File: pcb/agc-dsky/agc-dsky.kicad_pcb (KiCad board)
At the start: 2 copper layers, 100 x 115 mm, 152 parts, among them IC1 TPS62132, IC10 LDS-3161AX, IC11 LDS-3161AX, IC12 LDS-3161AX, IC13 LDS-3161AX, IC14 LDS-3161AX, IC15 LDS-3161AX, IC16 LDS-3161AX, IC17 LDS-3161AX, IC18 LDS-3161AX, IC19 LDS-3161AX, IC2 STM32F072RBT6, IC20 LDS-3161AX, IC21 LDS-3161AX, IC22 LDS-3161AX, IC23 LDS-3161AX, IC24 LDS-3161AX, IC25 LDS-3161AX, IC26 LDS-3161AX, IC27 WS2812B, IC28 WS2812B, IC29 WS2812B, IC3 MCP23S08, IC30 WS2812B, IC31 WS2812B, IC32 WS2812B, IC33 WS2812B, IC34 WS2812B, IC35 WS2812B, IC36 WS2812B, IC37 WS2812B, IC38 WS2812B, IC39 WS2812B, IC4 MCP23S08, IC5 MCP23S08, IC6 LDS-3161AX, IC7 LDS-3161AX, IC8 LDS-3161AX, IC9 LDS-3161AX, J1 MICROUSB, P1 SWD_TC, Q1 FDN327N, Q2 FDN327N, Q3 FDN327N, Q4 FDN327N, Q5 FDN327N, Q6 FDN327N, Q7 FDN327N, Q8 FDN327N, SW1 SKPMAME010, SW10 SKPMAME010, SW11 SKPMAME010, SW12 SKPMAME010, SW13 SKPMAME010, SW14 SKPMAME010, SW15 SKPMAME010, SW16 SKPMAME010, SW17 SKPMAME010, SW18 SKPMAME010, SW19 SKPMAME010, SW2 SKPMAME010, SW20 SKPMAME010, SW3 SKPMAME010, SW4 SKPMAME010, SW5 SKPMAME010, SW6 SKPMAME010, SW7 SKPMAME010, SW8 SKPMAME010, SW9 SKHHALA010

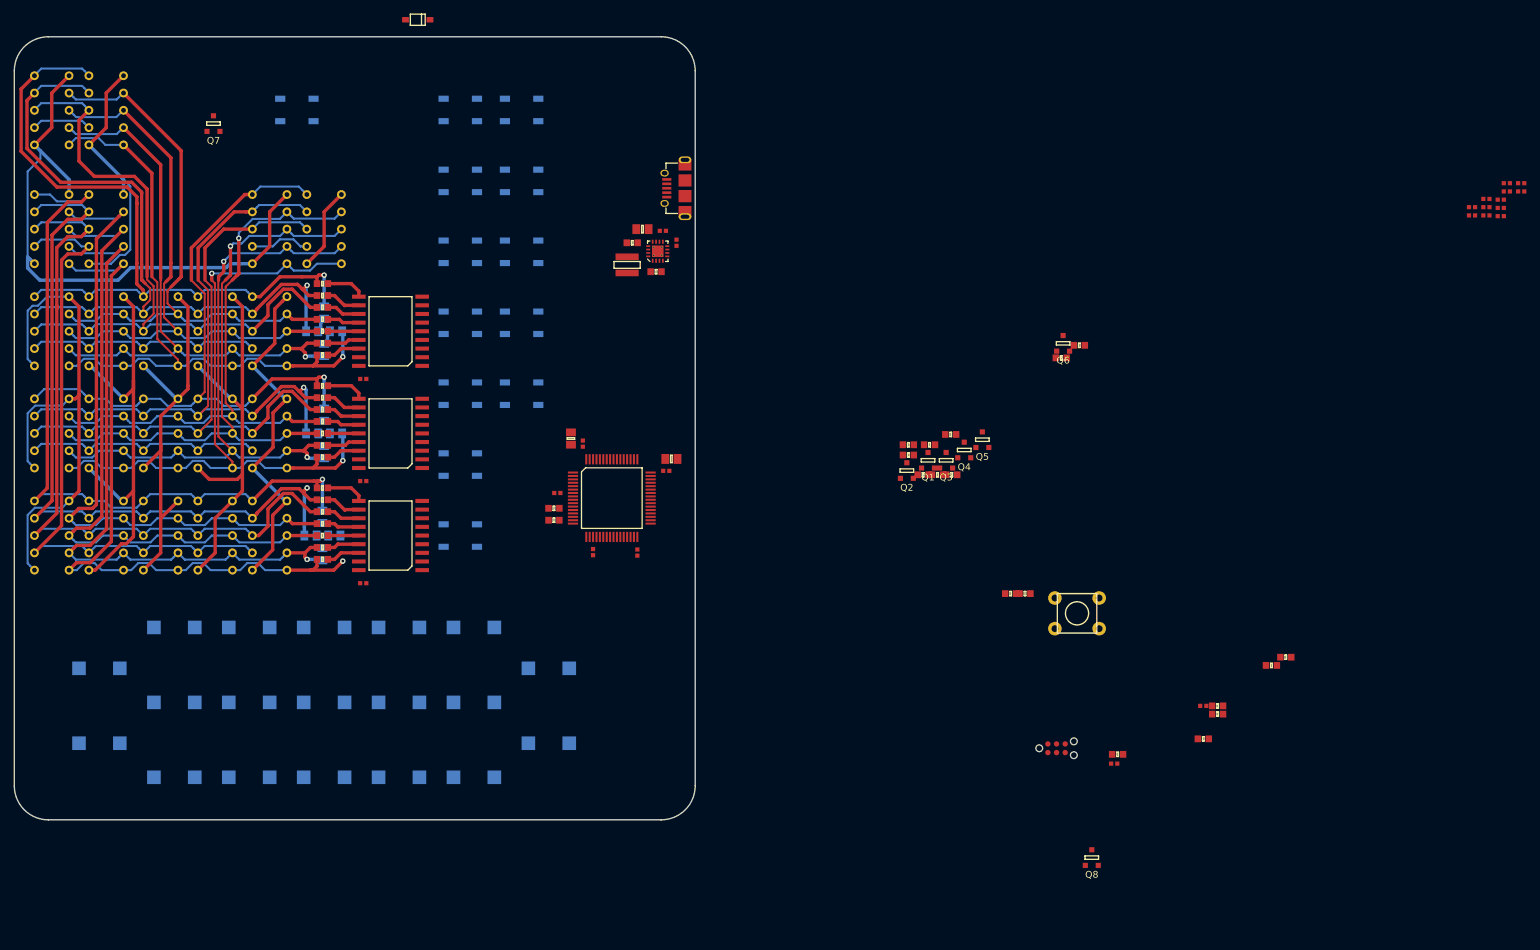
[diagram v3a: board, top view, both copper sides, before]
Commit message: Add ground pour on bottom layer
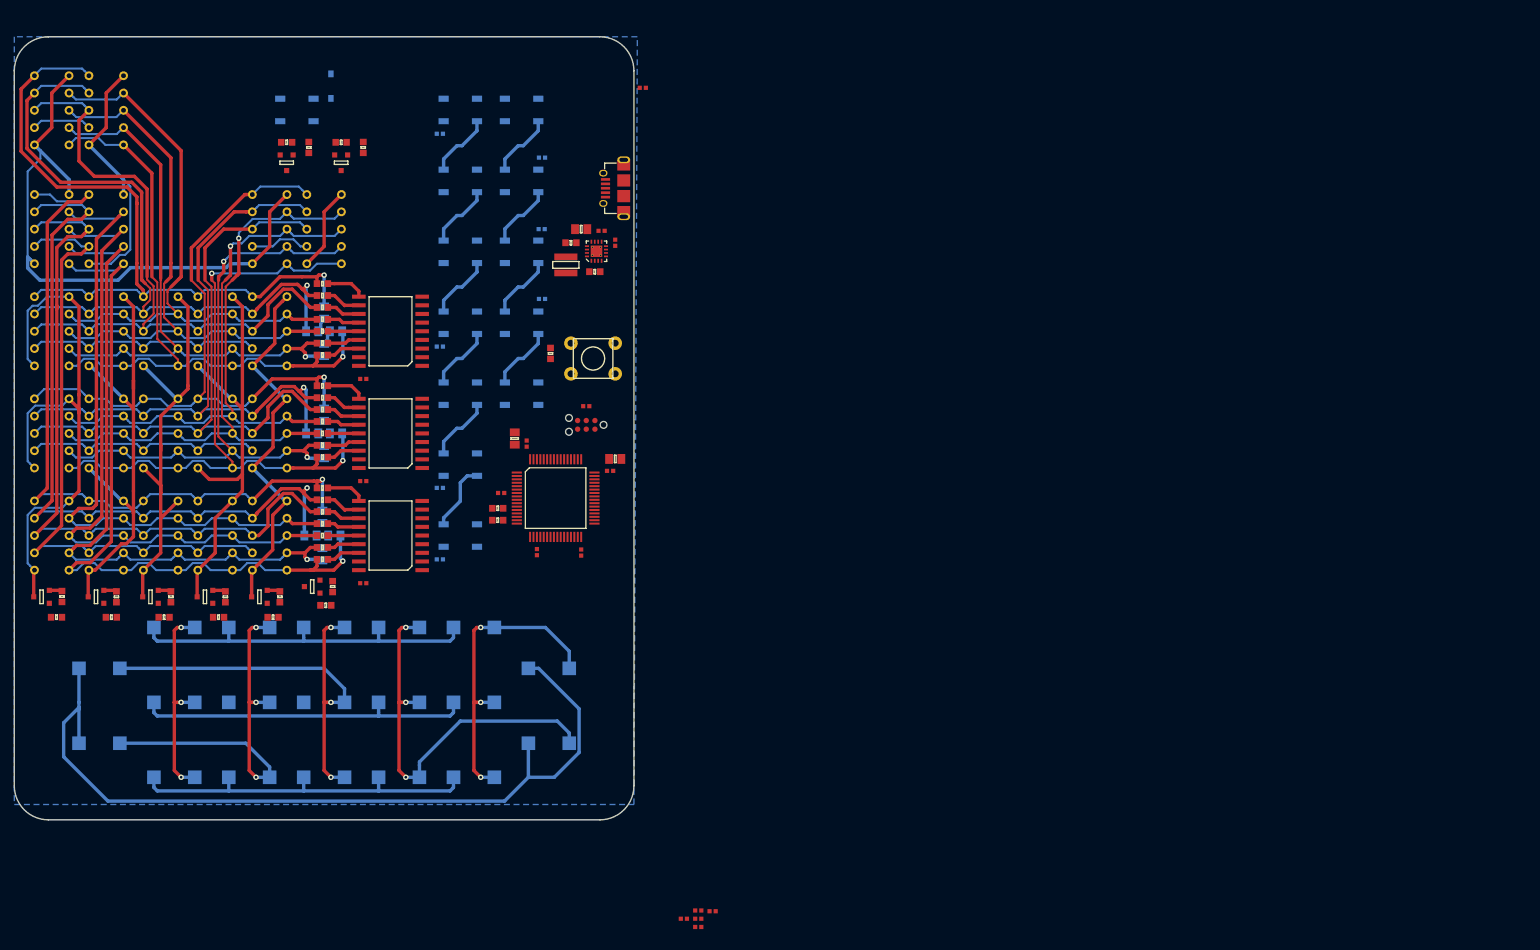
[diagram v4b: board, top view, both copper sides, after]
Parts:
- C19, C20, C21, C24, C25, C27, C30, D13: moved to B.Cu
- moved R30 170.5 mm to (73.0, 115.2), turned to 180 degrees
- moved C24 168.1 mm to (121.2, 106.8), turned to 180 degrees
- moved R29 164.0 mm to (81.8, 112.2), turned to 90 degrees
- moved C27 158.3 mm to (121.2, 75.5), turned to 180 degrees
- moved C30 156.9 mm to (121.2, 44.2), turned to 180 degrees
- moved C25 156.8 mm to (121.2, 96.2), turned to 180 degrees
- moved C23 155.9 mm to (159.2, 160.7)
- moved C22 155.9 mm to (161.3, 158.4)
- moved C26 155.9 mm to (159.2, 159.5)
- moved C29 155.9 mm to (159.2, 158.3)
- moved C28 155.9 mm to (157.1, 159.5)
- moved R28 153.7 mm to (80.8, 115.2)
- moved R27 146.6 mm to (89.8, 112.2), turned to 90 degrees
- moved C19 143.9 mm to (136.2, 47.8)
- moved C21 141.3 mm to (136.2, 68.5)
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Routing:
- net /BR4: track 0.00 -> 122.1 mm
- net /BC3: track 0.00 -> 66.4 mm, vias 0 -> 3
- net /BC2: track 0.00 -> 59.1 mm, vias 0 -> 3
- net /BC4: track 0.00 -> 55.1 mm, vias 0 -> 3
- net /BR3: track 0.00 -> 53.4 mm
- net /BR1: track 0.00 -> 53.4 mm
- net /BR2: track 0.00 -> 49.4 mm
- net /BC1: track 0.00 -> 45.1 mm, vias 0 -> 3
- net /BC5: track 0.00 -> 30.2 mm, vias 0 -> 3
- net Net-(IC33-Pad2): track 0.00 -> 9.99 mm
- net Net-(IC38-Pad2): track 0.00 -> 9.59 mm
- net Net-(IC37-Pad2): track 0.00 -> 9.59 mm
- net Net-(IC36-Pad2): track 0.00 -> 9.59 mm
- net Net-(IC35-Pad2): track 0.00 -> 9.59 mm
- net Net-(IC34-Pad2): track 0.00 -> 9.59 mm
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- added copper zone on B.Cu, net GND
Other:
- board size 100 x 115 mm -> 91 x 115 mm

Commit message: More work on layout
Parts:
- C18, C22, C23, C26, C28, C29: moved to B.Cu
- moved C23 135.4 mm to (104.2, 37.0), turned to 90 degrees
- moved C29 114.3 mm to (110.8, 54.8), turned to 180 degrees
- moved C28 105.2 mm to (110.8, 65.0), turned to 180 degrees
- moved C26 88.2 mm to (110.8, 85.8), turned to 180 degrees
- moved C22 83.4 mm to (136.7, 78.8)
- moved J1 60.0 mm to (148.2, 112.2)
- moved C18 14.8 mm to (136.2, 37.2)
- moved C11 14.5 mm to (140.2, 107.0)
- moved C8 14.1 mm to (143.8, 105.8), turned to 270 degrees
- moved C10 13.8 mm to (128.2, 104.8)
- moved C6 13.4 mm to (144.5, 94.5), turned to 0 degrees
- moved C30 12.5 mm to (108.8, 42.6)
- moved C24 11.9 mm to (109.6, 104.2), turned to 90 degrees
- moved C13 11.8 mm to (127.8, 96.8), turned to 180 degrees
- moved C7 11.7 mm to (143.8, 96.2), turned to 0 degrees
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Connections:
- C10 pad 2: Net-(C10-Pad2) -> GND
- C11 pad 2: Net-(C11-Pad2) -> GND
- C12 pad 2: Net-(C12-Pad2) -> GND
- C13 pad 2: Net-(C10-Pad2) -> GND
- C6 pad 2: Net-(C10-Pad2) -> GND
- C7 pad 2: Net-(C10-Pad2) -> GND
- C8 pad 2: Net-(C11-Pad2) -> GND
- C9 pad 2: Net-(C12-Pad2) -> GND
- IC2 pad 15: (no net) -> /NCS_2
- IC2 pad 16: (no net) -> /NRST_2
- IC2 pad 24: /NRST_1 -> (no net)
- IC2 pad 25: /NCS_1 -> (no net)
- IC2 pad 26: /NRST_2 -> (no net)
- IC2 pad 27: /NCS_2 -> (no net)
- IC2 pad 28: (no net) -> /NCS_3
- IC2 pad 29: /Co8 -> /NRST_3
- IC2 pad 3: (no net) -> /Co6
- IC2 pad 30: /NRST_3 -> /Co8
- IC2 pad 33: /NCS_3 -> (no net)
- IC2 pad 37: (no net) -> /Co1
- IC2 pad 38: (no net) -> /Co2
- IC2 pad 39: /BC1 -> /Co3
- IC2 pad 4: (no net) -> /Co7
- IC2 pad 40: /BC2 -> /Co4
- IC2 pad 41: /BC3 -> /Co5
- IC2 pad 42: /BC4 -> /BR2
- IC2 pad 43: /BC5 -> /BR4
- IC2 pad 50: (no net) -> /BR3
- IC2 pad 51: (no net) -> /BR1
- IC2 pad 55: /Co1 -> /BC5
- IC2 pad 56: /Co2 -> /BC4
- IC2 pad 57: /Co3 -> /BC3
- IC2 pad 58: /Co4 -> /BC2
- IC2 pad 59: /Co5 -> /BC1
- IC2 pad 61: /Co6 -> (no net)
- IC2 pad 62: /Co7 -> (no net)
- IC2 pad 8: (no net) -> /NCS_1
- IC2 pad 9: (no net) -> /NRST_1
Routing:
- net /BR4: track 122.1 -> 17.3 mm, vias 0 -> 1
- net /Co5: track 0.00 -> 79.1 mm
- net /Co4: track 0.00 -> 69.7 mm
- net /Co3: track 0.00 -> 60.6 mm
- net 5v: track 0.00 -> 51.6 mm
- net /Co2: track 0.00 -> 51.2 mm
- net /Co1: track 0.00 -> 42.4 mm
- net /SPI1_SI: track 0.00 -> 38.5 mm, vias 0 -> 2
- net /SPI1_SO: track 0.00 -> 38.1 mm
- net /BC2: track 59.1 -> 24.1 mm, vias 3 -> 0
- net /SPI1_SCK: track 0.00 -> 32.9 mm
- net /NCS_1: track 0.00 -> 31.0 mm
- net /NRST_1: track 0.00 -> 30.2 mm
- net /Co8: track 0.00 -> 29.4 mm
- net /BR2: track 49.4 -> 78.6 mm, vias 0 -> 1
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
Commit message: More routing of buttons
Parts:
- moved SW1 4.75 mm to (126.2, 121.5)
- moved SW10 4.75 mm to (104.2, 121.5)
- moved SW11 4.75 mm to (104.2, 132.5)
- moved SW12 4.75 mm to (104.2, 143.5)
- moved SW13 4.75 mm to (71.2, 127.5)
- moved SW14 4.75 mm to (93.2, 121.5)
- moved SW15 4.75 mm to (93.2, 132.5)
- moved SW16 4.75 mm to (93.2, 143.5)
- moved SW17 4.75 mm to (71.2, 138.5)
- moved SW18 4.75 mm to (82.2, 121.5)
- moved SW19 4.75 mm to (82.2, 132.5)
- moved SW2 4.75 mm to (126.2, 132.5)
- moved SW20 4.75 mm to (82.2, 143.5)
- moved SW3 4.75 mm to (126.2, 143.5)
- moved SW4 4.75 mm to (137.2, 127.5)
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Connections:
- IC2 pad 55: /BC5 -> /BC3
- IC2 pad 56: /BC4 -> /BC1
- IC2 pad 57: /BC3 -> /BC2
- IC2 pad 58: /BC2 -> /BC4
- IC2 pad 59: /BC1 -> /BC5
- SW13 pad 1: /BC3 -> /BC5
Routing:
- net /BR4: track 17.3 -> 132.5 mm, vias 1 -> 3
- net /BC2: track 24.1 -> 111.0 mm, vias 0 -> 1
- net /BC5: track 28.7 -> 114.2 mm, vias 3 -> 1
- net /BC4: track 41.4 -> 117.6 mm, vias 2 -> 1
- net /BC1: track 16.4 -> 73.2 mm, vias 2 -> 1
- net /BR3: track 66.7 -> 120.7 mm, vias 3 -> 7
- net /BC3: track 52.7 -> 87.3 mm, vias 2 -> 1
- net /BR1: track 66.4 -> 95.1 mm, vias 2 -> 7
- net /BR2: track 78.6 -> 99.5 mm, vias 1 -> 5
- net /SWDCLK: track 11.5 -> 0.00 mm
- net 3v3: track 11.4 -> 22.2 mm, vias 0 -> 2
- net /Co8: track 29.4 -> 31.0 mm
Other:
- board size 91 x 115 mm -> 91 x 120 mm

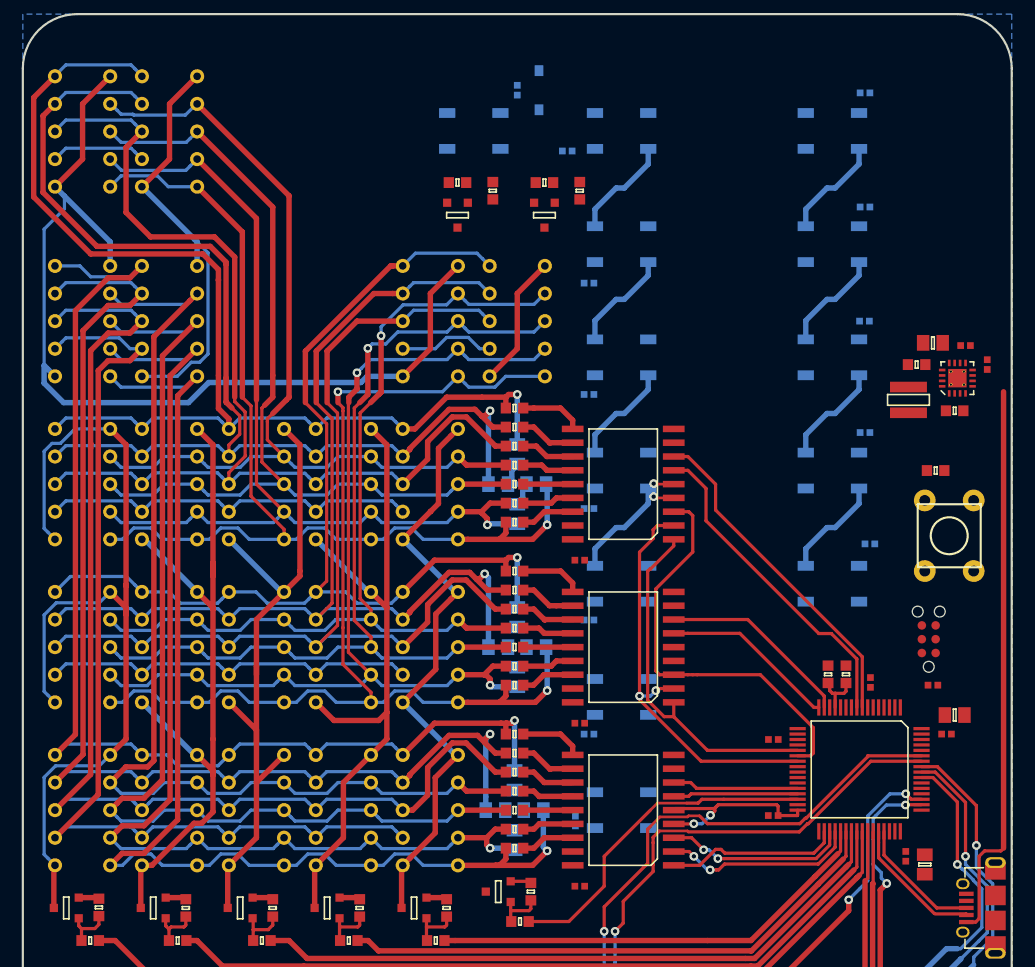
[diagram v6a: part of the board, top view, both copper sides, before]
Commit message: First routing attempt
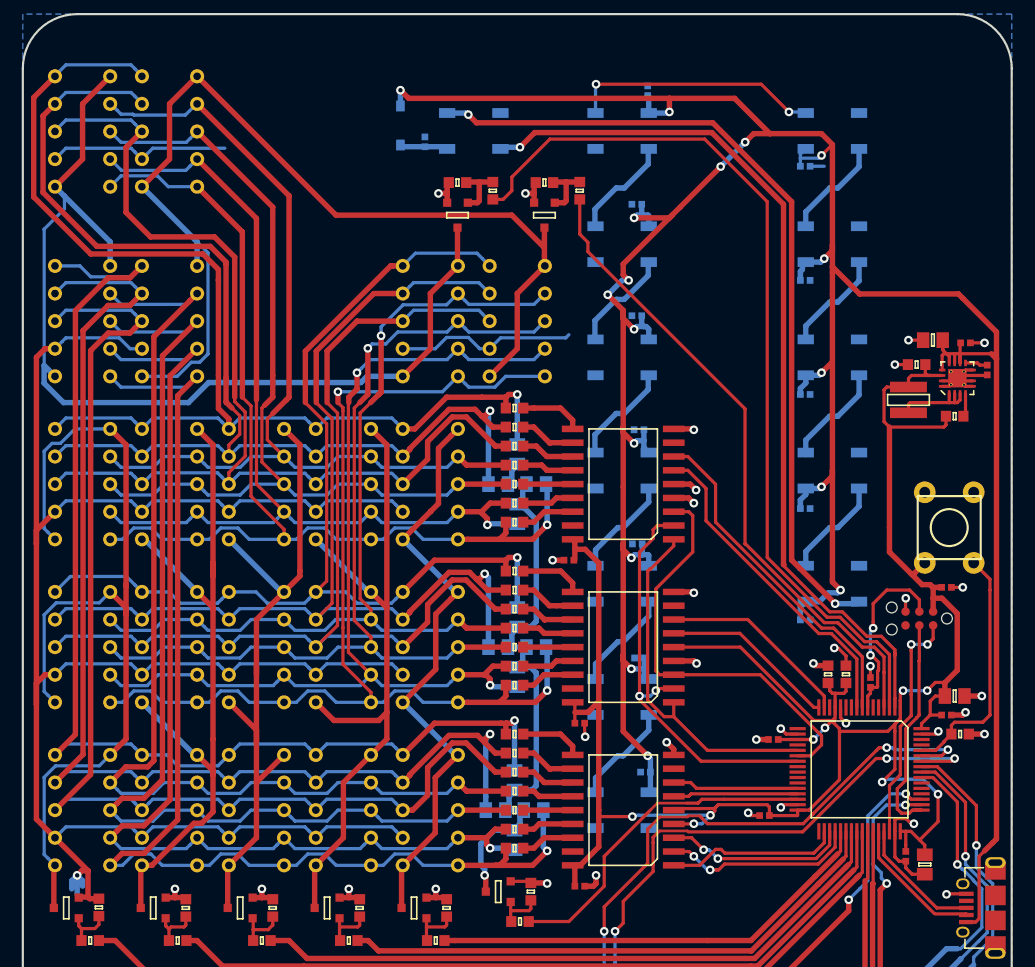
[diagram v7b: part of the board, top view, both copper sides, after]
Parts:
- KEY REL: renamed from SW20
- moved IC33 62.5 mm to (113.9, 40.8), turned to 180 degrees
- moved IC39 62.5 mm to (113.9, 103.2), turned to 180 degrees
- moved IC34 41.7 mm to (113.9, 51.2), turned to 180 degrees
- moved IC38 41.7 mm to (113.9, 92.8), turned to 180 degrees
- moved IC28 41.7 mm to (133.2, 82.4), turned to 0 degrees
- moved IC32 41.7 mm to (133.2, 40.8), turned to 0 degrees
- moved R2 24.4 mm to (145.0, 96.2)
- moved IC35 20.8 mm to (113.9, 61.6), turned to 180 degrees
- moved IC37 20.8 mm to (113.9, 82.4), turned to 180 degrees
- moved IC29 20.8 mm to (133.2, 72.0), turned to 0 degrees
- moved IC31 20.8 mm to (133.2, 51.2), turned to 0 degrees
- moved D13 13.2 mm to (93.5, 40.2)
- moved C23 9.74 mm to (95.8, 41.8)
- moved C30 9.25 mm to (116.2, 37.0), turned to 90 degrees
- moved C22 9.19 mm to (130.8, 85.8)
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- renumbered SW1 to +, SW2 to -, SW3 to 0, SW7 to 1, SW12 to 2, SW16 to 3, SW6 to 4, SW11 to 5, SW15 to 6, SW5 to 7, SW10 to 8, SW14 to 9, SW18 to CLR, SW13 to ENTR, SW8 to NOUN, SW19 to PRO, SW17 to RSET, SW4 to VERB
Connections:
- IC2 pad 3: /Co6 -> /Co7
- IC2 pad 4: /Co7 -> /Co6
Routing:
- net 5v: track 51.6 -> 300.1 mm, vias 0 -> 17
- net 3v3: track 22.2 -> 200.7 mm, vias 2 -> 9
- net GND: track 197.2 -> 298.0 mm, vias 2 -> 36
- net /Co7: track 0.00 -> 83.2 mm
- net /LED_DIN: track 0.00 -> 81.7 mm, vias 0 -> 1
- net Net-(IC27-Pad2): track 0.00 -> 76.0 mm, vias 0 -> 2
- net /Co6: track 0.00 -> 59.8 mm
- net Net-(D1-Pad1): track 6.10 -> 54.7 mm, vias 0 -> 1
- net Net-(IC21-Pad1): track 51.9 -> 94.7 mm
- net Net-(IC32-Pad2): track 0.00 -> 23.1 mm, vias 0 -> 2
- net Net-(IC2-Pad60): track 0.00 -> 22.8 mm
- net /SWDIO: track 0.00 -> 21.5 mm, vias 0 -> 2
- net /SWDCLK: track 0.00 -> 20.9 mm
- net /NRST: track 0.00 -> 17.0 mm, vias 0 -> 2
- net Net-(IC34-Pad2): track 0.00 -> 9.59 mm
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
